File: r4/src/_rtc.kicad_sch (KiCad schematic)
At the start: 8 parts, among them U13 DS3231MZ, U14 74LVC1G07DCK

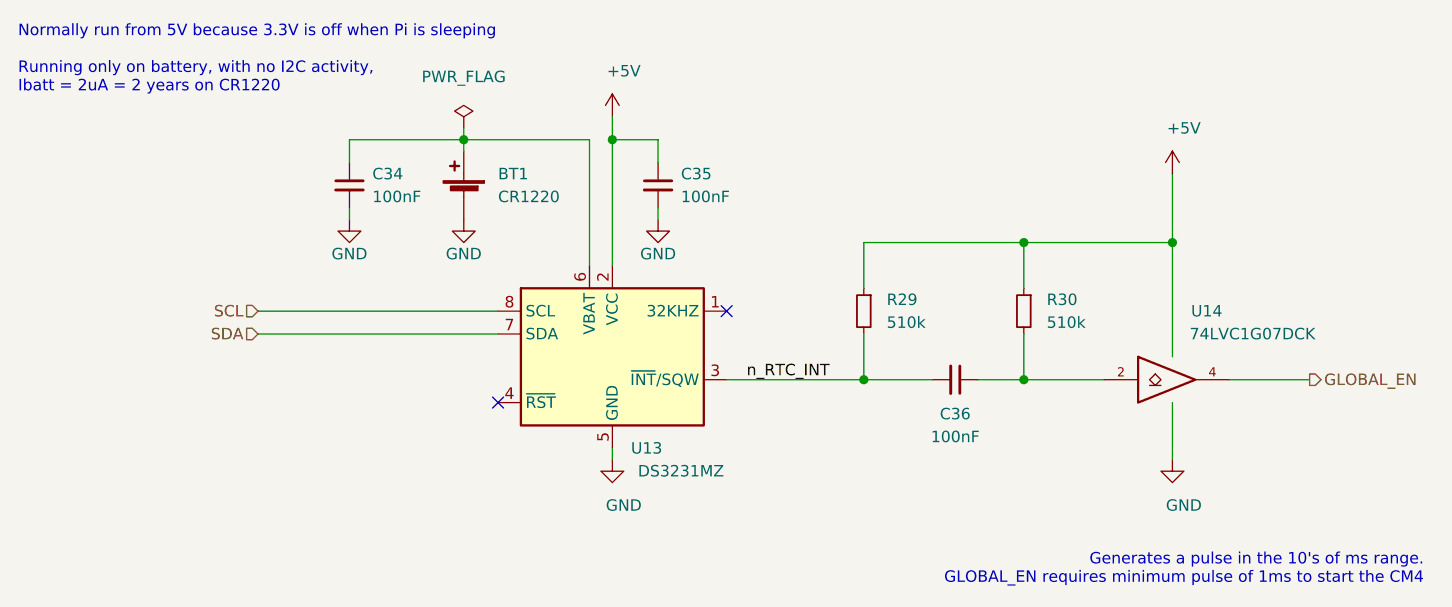
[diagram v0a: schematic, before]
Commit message: Update files to Kicad 6 format
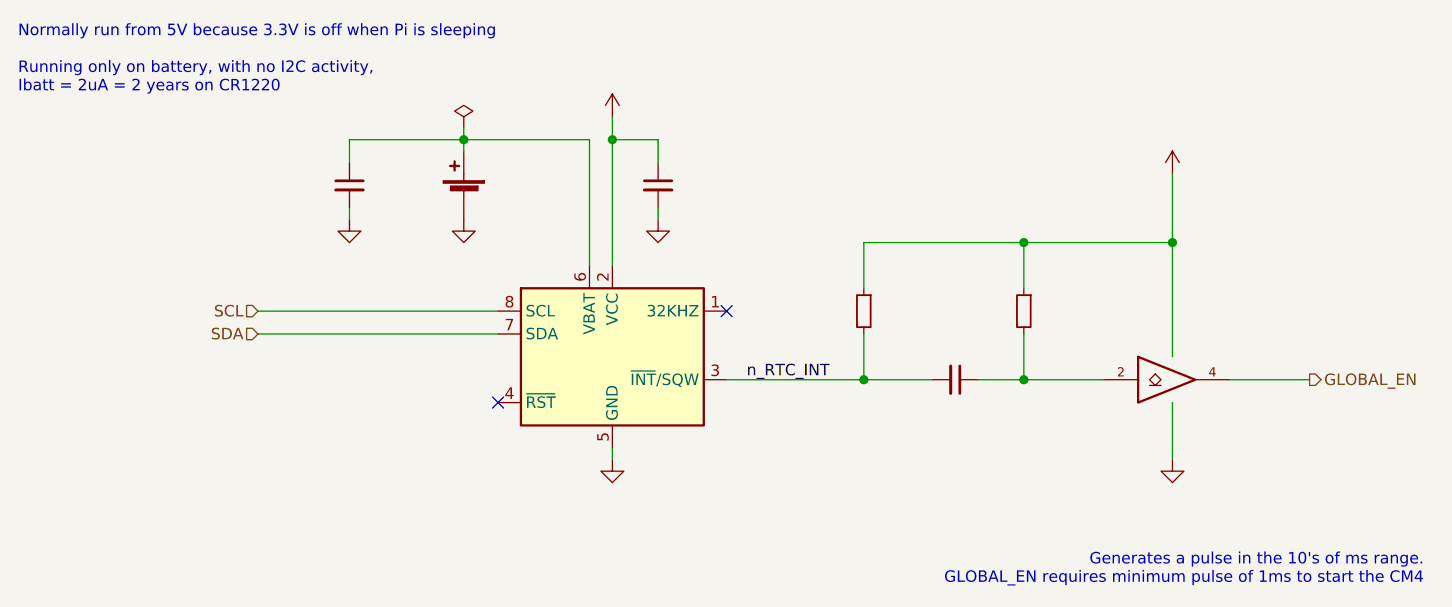
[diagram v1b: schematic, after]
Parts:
- ?: renamed from C35; value 100nF -> (none); footprint Capacitor_SMD:C_0603_1608Metric -> (none)
- ?: renamed from U14; value 74LVC1G07DCK -> (none); footprint Package_TO_SOT_SMD:SOT-353_SC-70-5 -> (none)
- ?: renamed from BT1; value CR1220 -> (none); footprint jeffmakes-footprints:Keystone-3000-CR1220-CR1216 -> (none)
- ?: renamed from C36; value 100nF -> (none); footprint Capacitor_SMD:C_0603_1608Metric -> (none)
- ?: renamed from R30; value 510k -> (none); footprint Resistor_SMD:R_0603_1608Metric -> (none)
- ?: renamed from R29; value 510k -> (none); footprint Resistor_SMD:R_0603_1608Metric -> (none)
- ?: renamed from U13; value DS3231MZ -> (none); footprint Package_SO:SOIC-8_3.9x4.9mm_P1.27mm -> (none)
- ?: renamed from C34; value 100nF -> (none); footprint Capacitor_SMD:C_0603_1608Metric -> (none)

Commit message: Add TVS diode to RTC battery connection
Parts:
- added ?: (no value), symbol Device:D_TVS
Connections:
- net GND: now also ?.1 (A1)
- net at ?.1, ?.1 (+), ?.6 (VBAT): now also ?.2 (A2)
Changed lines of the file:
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@@
   (junction (at 106.68 72.39) (diameter 1.016) (color 0 0 0 0)
+  )
+  (junction (at 93.98 72.39) (diameter 0) (color 0 0 0 0)
   )
   (junction (at 168.91 83.82) (diameter 1.016) (color 0 0 0 0)
@@
   (wire (pts (xy 168.91 99.06) (xy 177.8 99.06))
     (stroke (width 0) (type solid))
+  )
+  (wire (pts (xy 93.98 72.39) (xy 82.55 72.39))
+    (stroke (width 0) (type default))
   )
   (wire (pts (xy 120.65 72.39) (xy 120.65 86.36))
@@
     (stroke (width 0) (type solid))
   )
+  (wire (pts (xy 82.55 72.39) (xy 82.55 73.66))
+    (stroke (width 0) (type default))
+  )
   (wire (pts (xy 128.27 81.28) (xy 128.27 80.01))
     (stroke (width 0) (type solid))
@@
     (effects (font (size 1.27 1.27)) (justify left))
   )
+  (symbol (lib_id "power:GND") (at 82.55 81.28 0) (unit 1)
+    (in_bom yes) (on_board yes) (dnp no)
+    (default_instance (reference "") (unit 1) (value "") (footprint ""))
+    (property "Reference" "" (at 82.55 87.63 0)
+      (effects (font (size 1.27 1.27)) hide)
+    )
+    (property "Value" "" (at 82.55 85.09 0)
+      (effects (font (size 1.27 1.27)))
+    )
+    (property "Footprint" "" (at 82.55 81.28 0)
+      (effects (font (size 1.27 1.27)) hide)
+    )
+    (property "Datasheet" "" (at 82.55 81.28 0)
+      (effects (font (size 1.27 1.27)) hide)
+    )
+    (pin "1")
+  )
+  (symbol (lib_id "Device:D_TVS") (at 82.55 77.47 270) (mirror x) (unit 1)
+    (in_bom yes) (on_board yes) (dnp no)
+    (default_instance (reference "") (unit 1) (value "") (footprint ""))
+    (property "Reference" "" (at 86.36 82.55 0)
+      (effects (font (size 1.27 1.27)) (justify right))
+    )
+    (property "Value" "" (at 88.9 73.66 0)
+      (effects (font (size 1.27 1.27)) (justify right))
+    )
+    (property "Footprint" "" (at 82.55 77.47 0)
+      (effects (font (size 1.27 1.27)) hide)
+    )
+    (property "Datasheet" "~" (at 82.55 77.47 0)
+      (effects (font (size 1.27 1.27)) hide)
+    )
+    (pin "1")
+    (pin "2")
+  )
   (symbol (lib_id "power:GND") (at 123.19 107.95 0) (unit 1)

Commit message: Add netclass definitions and assign nets. Define DRC rules to each class. Resize all vias and nets (with a few exceptions for very wide power tracks) to follow the netclass rules. Increase area for GNDA domain. Re-route SIM data bus around edge of GNDA domain
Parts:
- BT1: renamed from ?; value (none) -> CR1220; footprint (none) -> jeffmakes-footprints:Keystone-3000-CR1220-CR1216
- C34, C35, C36: renamed from ?; value (none) -> 100nF; footprint (none) -> Capacitor_SMD:C_0603_1608Metric
- D20: renamed from ?; value (none) -> 0402ESDA-MLP1; footprint (none) -> Diode_SMD:D_0402_1005Metric
- R29, R30: renamed from ?; value (none) -> 510k; footprint (none) -> Resistor_SMD:R_0603_1608Metric
- U13: renamed from ?; value (none) -> DS3231MZ; footprint (none) -> Package_SO:SOIC-8_3.9x4.9mm_P1.27mm
- U14: renamed from ?; value (none) -> 74LVC1G07DCK; footprint (none) -> Package_TO_SOT_SMD:SOT-353_SC-70-5

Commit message: File noise due to Kicad version bump
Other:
- note added: "Address 110 1000 (0x68)"
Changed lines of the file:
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@@
-(kicad_sch (version 20221004) (generator eeschema)
+(kicad_sch (version 20230409) (generator eeschema)
   (paper "A4")
   (junction (at 123.19 72.39) (diameter 1.016) (color 0 0 0 0)
@@
     (stroke (width 0) (type solid))
   )
-  (text "Generates a pulse in the 10's of ms range. \nGLOBAL_EN requires minimum pulse of 1ms to start the CM4"
+  (text "Generates a pulse in the 10's of ms range. \nGLOBAL_EN requires minimum pulse of 1ms to start the CM4" (exclude_from_sim no)
     (at 213.36 121.92 0)
     (effects (font (size 1.27 1.27)) (justify right bottom))
   )
-  (text "Normally run from 5V because 3.3V is off when Pi is sleeping\n\nRunning only on battery, with no I2C activity, \nIbatt = 2uA = 2 years on CR1220"
+  (text "Address 110 1000 (0x68)" (exclude_from_sim no)
+ (at 104.14 111.76 0)
+    (effects (font (size 1.27 1.27)) (justify right bottom))
+  )
+  (text "Normally run from 5V because 3.3V is off when Pi is sleeping\n\nRunning only on battery, with no I2C activity, \nIbatt = 2uA = 2 years on CR1220" (exclude_from_sim no)
     (at 57.15 67.31 0)
     (effects (font (size 1.27 1.27)) (justify left bottom))
@@
       (project "bugg-main-r4"
         (path "/e3eb514f-6ce4-4abe-ba20-f82f0015628f/41dcda57-f03b-4254-a26d-4b483d171c17"
-          (reference "#PWR098") (unit 1) (value "GND") (footprint "")
+          (reference "#PWR098") (unit 1)
         )
       )
@@
       (project "bugg-main-r4"
         (path "/e3eb514f-6ce4-4abe-ba20-f82f0015628f/41dcda57-f03b-4254-a26d-4b483d171c17"
-          (reference "D20") (unit 1) (value "0402ESDA-MLP1") (footprint "Diode_SMD:D_0402_1005Metric")
+          (reference "D20") (unit 1)
         )
       )
@@
       (project "bugg-main-r4"
         (path "/e3eb514f-6ce4-4abe-ba20-f82f0015628f/41dcda57-f03b-4254-a26d-4b483d171c17"
-          (reference "#PWR0101") (unit 1) (value "GND") (footprint "")
+          (reference "#PWR0101") (unit 1)
         )
       )
@@
       (project "bugg-main-r4"
         (path "/e3eb514f-6ce4-4abe-ba20-f82f0015628f/41dcda57-f03b-4254-a26d-4b483d171c17"
-          (reference "#PWR0103") (unit 1) (value "+5V") (footprint "")
+          (reference "#PWR0103") (unit 1)
         )
       )
@@
       (project "bugg-main-r4"
         (path "/e3eb514f-6ce4-4abe-ba20-f82f0015628f/41dcda57-f03b-4254-a26d-4b483d171c17"
-          (reference "#PWR0139") (unit 1) (value "GND") (footprint "")
+          (reference "#PWR0139") (unit 1)
         )
       )
@@
       (project "bugg-main-r4"
         (path "/e3eb514f-6ce4-4abe-ba20-f82f0015628f/41dcda57-f03b-4254-a26d-4b483d171c17"
-          (reference "#PWR0104") (unit 1) (value "GND") (footprint "")
+          (reference "#PWR0104") (unit 1)
         )
       )
@@
       (project "bugg-main-r4"
         (path "/e3eb514f-6ce4-4abe-ba20-f82f0015628f/41dcda57-f03b-4254-a26d-4b483d171c17"
-          (reference "C35") (unit 1) (value "100nF") (footprint "Capacitor_SMD:C_0603_1608Metric")
+          (reference "C35") (unit 1)
         )
       )
@@
       (project "bugg-main-r4"
         (path "/e3eb514f-6ce4-4abe-ba20-f82f0015628f/41dcda57-f03b-4254-a26d-4b483d171c17"
-          (reference "U14") (unit 1) (value "74LVC1G07DCK") (footprint "Package_TO_SOT_SMD:SOT-353_SC-70-5")
+          (reference "U14") (unit 1)
         )
       )
@@
       (project "bugg-main-r4"
         (path "/e3eb514f-6ce4-4abe-ba20-f82f0015628f/41dcda57-f03b-4254-a26d-4b483d171c17"
-          (reference "BT1") (unit 1) (value "CR1220") (footprint "jeffmakes-footprints:Keystone-3000-CR1220-CR1216")
+          (reference "BT1") (unit 1)
         )
       )
@@
       (project "bugg-main-r4"
         (path "/e3eb514f-6ce4-4abe-ba20-f82f0015628f/41dcda57-f03b-4254-a26d-4b483d171c17"
-          (reference "#PWR0100") (unit 1) (value "+5V") (footprint "")
+          (reference "#PWR0100") (unit 1)
         )
       )
@@
       (project "bugg-main-r4"
         (path "/e3eb514f-6ce4-4abe-ba20-f82f0015628f/41dcda57-f03b-4254-a26d-4b483d171c17"
-          (reference "C36") (unit 1) (value "100nF") (footprint "Capacitor_SMD:C_0603_1608Metric")
+          (reference "C36") (unit 1)
         )
       )
@@
       (project "bugg-main-r4"
         (path "/e3eb514f-6ce4-4abe-ba20-f82f0015628f/41dcda57-f03b-4254-a26d-4b483d171c17"
-          (reference "#PWR099") (unit 1) (value "GND") (footprint "")
+          (reference "#PWR099") (unit 1)
         )
       )
@@
       (project "bugg-main-r4"
         (path "/e3eb514f-6ce4-4abe-ba20-f82f0015628f/41dcda57-f03b-4254-a26d-4b483d171c17"
-          (reference "R30") (unit 1) (value "510k") (footprint "Resistor_SMD:R_0603_1608Metric")
+          (reference "R30") (unit 1)
         )
       )
@@
       (project "bugg-main-r4"
         (path "/e3eb514f-6ce4-4abe-ba20-f82f0015628f/41dcda57-f03b-4254-a26d-4b483d171c17"
-          (reference "R29") (unit 1) (value "510k") (footprint "Resistor_SMD:R_0603_1608Metric")
+          (reference "R29") (unit 1)
         )
       )
@@
       (project "bugg-main-r4"
         (path "/e3eb514f-6ce4-4abe-ba20-f82f0015628f/41dcda57-f03b-4254-a26d-4b483d171c17"
-          (reference "#FLG0105") (unit 1) (value "PWR_FLAG") (footprint "")
+          (reference "#FLG0105") (unit 1)
         )
       )
@@
       (project "bugg-main-r4"
         (path "/e3eb514f-6ce4-4abe-ba20-f82f0015628f/41dcda57-f03b-4254-a26d-4b483d171c17"
-          (reference "U13") (unit 1) (value "DS3231MZ") (footprint "Package_SO:SOIC-8_3.9x4.9mm_P1.27mm")
+          (reference "U13") (unit 1)
         )
       )
@@
       (project "bugg-main-r4"
         (path "/e3eb514f-6ce4-4abe-ba20-f82f0015628f/41dcda57-f03b-4254-a26d-4b483d171c17"
-          (reference "#PWR0102") (unit 1) (value "GND") (footprint "")
+          (reference "#PWR0102") (unit 1)
         )
       )
@@
       (project "bugg-main-r4"
         (path "/e3eb514f-6ce4-4abe-ba20-f82f0015628f/41dcda57-f03b-4254-a26d-4b483d171c17"
-          (reference "C34") (unit 1) (value "100nF") (footprint "Capacitor_SMD:C_0603_1608Metric")
-        )
-      )
+          (reference "C34") (unit 1)
+        )
+      )
